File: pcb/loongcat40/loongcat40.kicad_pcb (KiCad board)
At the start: 2 copper layers, 219.1 x 76.2 mm, 91 parts, among them SW1 SW_Push, SW10 SW_Push, SW11 SW_Push, SW12 SW_Push, SW13 SW_Push, SW14 SW_Push, SW15 SW_Push, SW16 SW_Push, SW17 SW_Push, SW18 SW_Push, SW19 SW_Push, SW2 SW_Push, SW20 SW_Push, SW21 SW_Push, SW22 SW_Push, SW23 SW_Push, SW24 SW_Push, SW25 SW_Push, SW26 SW_Push, SW27 SW_Push, SW28 SW_Push, SW29 SW_Push, SW3 SW_Push, SW30 SW_Push, SW31 SW_Push, SW32 SW_Push, SW33 SW_Push, SW34 SW_Push, SW35 SW_Push, SW36 SW_Push, SW37 SW_Push, SW38 SW_Push, SW39 SW_Push, SW4 SW_Push, SW40 SW_Push, SW41 SW_Push, SW42 SW_Push, SW5 SW_Push, SW6 SW_Push, SW7 SW_Push, SW8 SW_Push, SW9 SW_Push

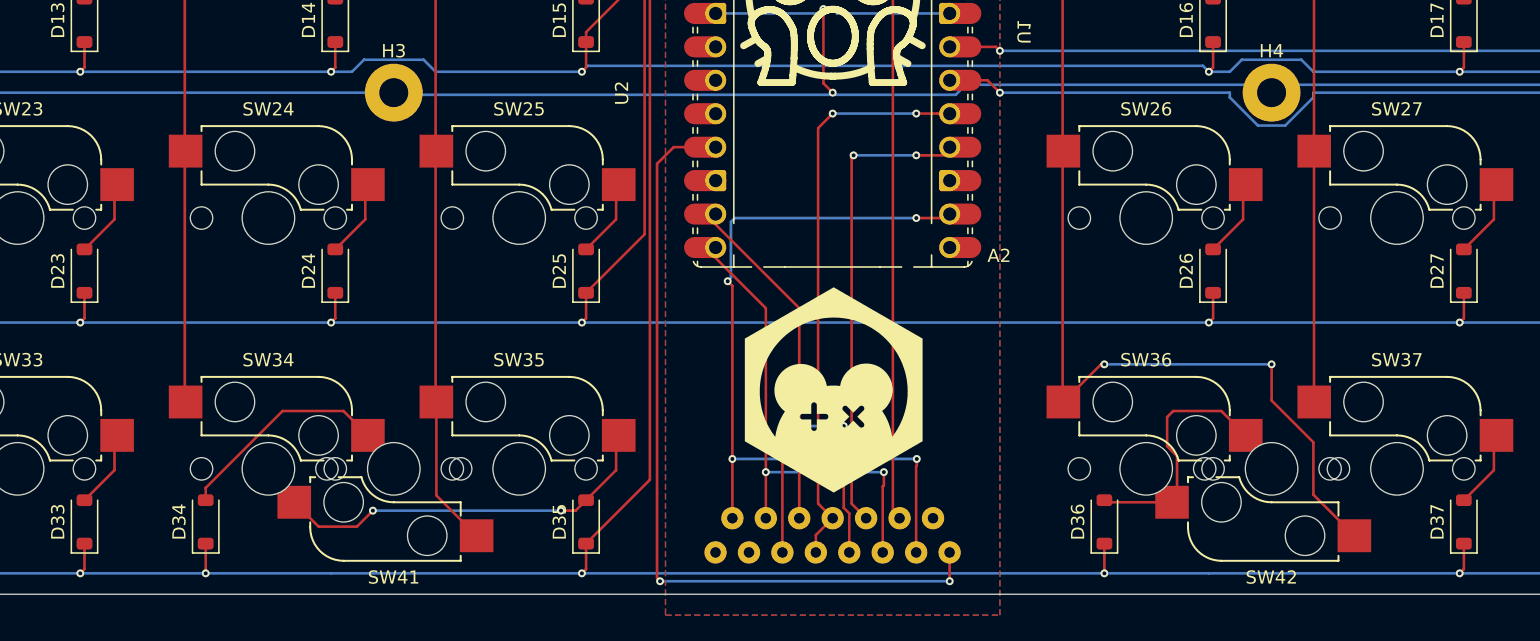
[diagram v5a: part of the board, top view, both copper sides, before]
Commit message: update pcb to support 2U stabilizers, update col10 pin
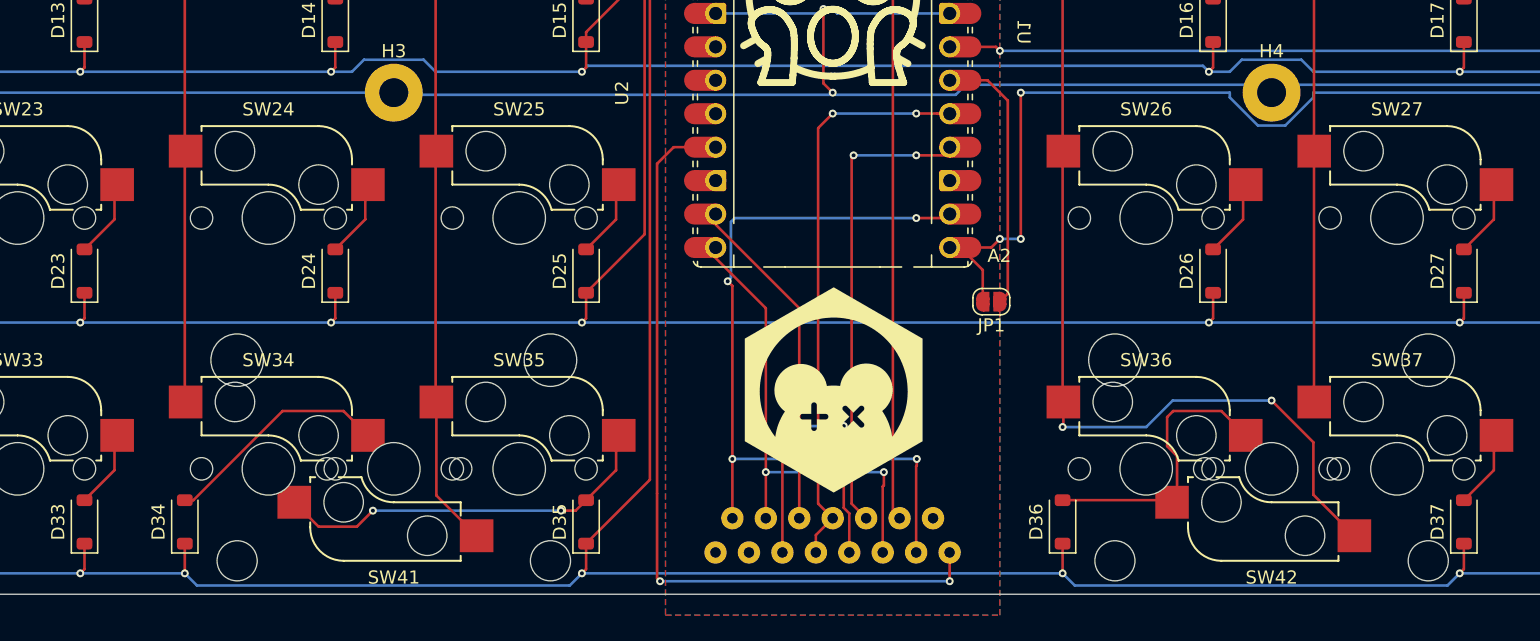
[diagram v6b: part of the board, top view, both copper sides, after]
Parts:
- added JP1: Jumper_2_Small_Open, Jumper:SolderJumper-2_P1.3mm_Open_RoundedPad1.0x1.5mm, F.Cu at (150.2, 82.5)
- added REF**: Stabilizer_MX_2u, keyswitches:Stabilizer_MX_2u, F.Cu at (171.4, 95.2)
- added REF**: Stabilizer_MX_2u, keyswitches:Stabilizer_MX_2u, F.Cu at (104.8, 95.2)
- moved D36 3.18 mm to (155.6, 99.3)
- moved D34 1.59 mm to (88.9, 99.3)
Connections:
- A2 pad 21: unconnected-(A2-GPIO16-Pad21)_1 -> COL_10
- A2 pad 26: COL_10 -> Net-(A2-GPIO20)
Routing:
- net Net-(A2-GPIO20): track 0.00 -> 19.8 mm
- net COL_10: track 144.2 -> 160.0 mm, vias 2 -> 4
- net Net-(D36-A): track 19.1 -> 22.3 mm
- net ROW_4: track 272.2 -> 273.7 mm
- net COL_6: track 98.9 -> 97.8 mm
- net Net-(D34-A): track 16.4 -> 17.5 mm
